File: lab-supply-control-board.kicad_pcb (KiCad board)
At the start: 2 copper layers, 94 x 66 mm, 101 parts, among them J1 0.1" header, J10 USB_B_Micro, J11 0.1" Header, J12 1x04 JST, J13 1x04 JST, J14 0.1" Header, J4 0.1" Header, J5 0.1" Header, J6 AVR-ISP-6, J7 0.1" Header, J8 0.1" Header, J9 0.1" Header, Q1 BSS138, Q2 BSS138, Q3 2N3904, Q4 2N3904, Q5 2N3904, Q6 BSS138, Q7 BSS138, U1 MCP4716AxT-ECH, U2 ATmega328P-AU, U3 24LC04, U4 LM4040DBZ-2.5, U5 MCP4716AxT-ECH, U6 MIC5365-3.3YD5, U7 FT232RL, Y1 Crystal_GND24

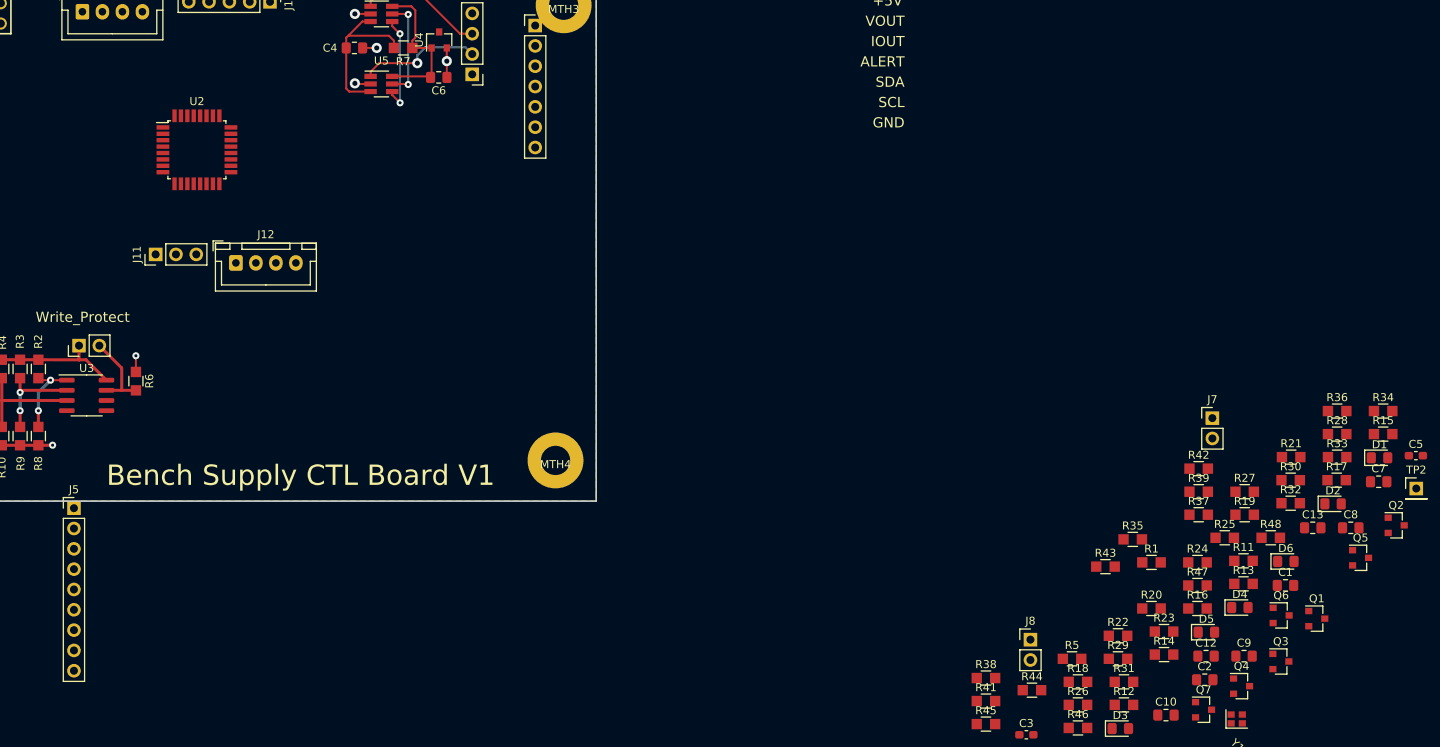
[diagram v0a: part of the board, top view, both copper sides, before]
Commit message: schematic tweak
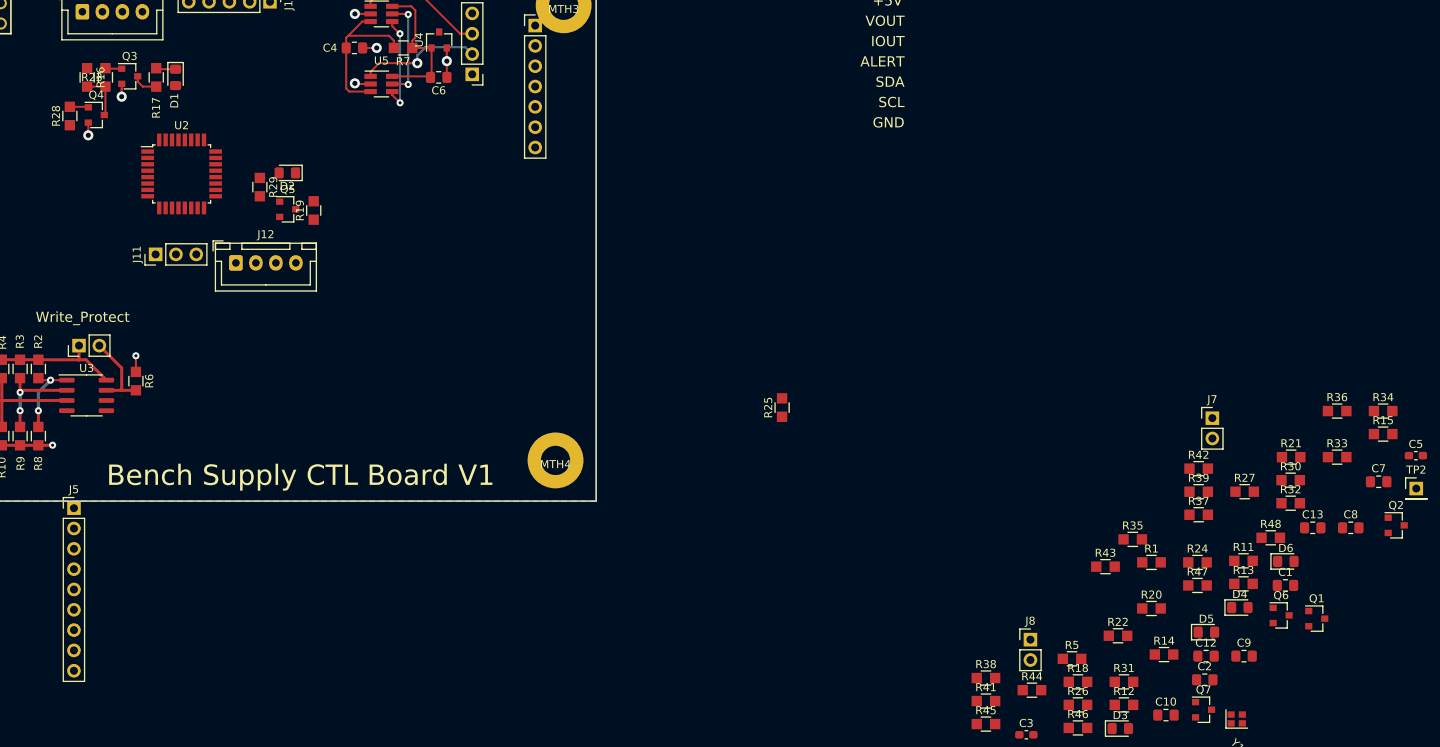
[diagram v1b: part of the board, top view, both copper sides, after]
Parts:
- moved R28 163.3 mm to (101.9, 71.2), turned to 90 degrees
- moved Q3 161.4 mm to (109.3, 66.3)
- moved Q4 160.0 mm to (105.2, 71.1)
- moved D1 157.8 mm to (115.1, 66.4), turned to 270 degrees
- moved R17 155.9 mm to (112.6, 66.4), turned to 90 degrees
- moved R16 153.9 mm to (104.0, 66.4), turned to 270 degrees
- moved R23 149.4 mm to (106.3, 66.4), turned to 90 degrees
- moved Q5 141.0 mm to (129.1, 82.9)
- moved D2 137.1 mm to (129.0, 78.4), turned to 180 degrees
- moved R19 122.4 mm to (132.3, 83.1), turned to 90 degrees
- moved R29 122.4 mm to (125.6, 80.1), turned to 270 degrees
- moved R25 57.7 mm to (190.9, 107.7), turned to 90 degrees
- moved U2 3.57 mm to (115.8, 78.5)
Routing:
- net Net-(Q4-Pad3): track 0.00 -> 5.89 mm
- net Net-(Q3-Pad3): track 0.00 -> 3.23 mm
- net GND: track 17.8 -> 21.0 mm, vias 6 -> 8
- net Net-(D1-Pad1): track 0.00 -> 2.46 mm
- net Net-(Q4-Pad2): track 0.00 -> 2.33 mm
- net Net-(Q3-Pad2): track 0.00 -> 2.06 mm

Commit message: Updates to schematic, started control board layout
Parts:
- removed C10, C9: 1.0u, Rays Footprints:C_0805_HandSoldering
- removed Q1, Q2, Q6: BSS138, Package_TO_SOT_SMD:SOT-23
- removed R11, R12, R13, R14, R34, R35: 10k, Rays Footprints:R_0805_HandSoldering
- removed U6: MIC5365-3.3YD5, Package_TO_SOT_SMD:SOT-23-5
- added C14: 0.1u, Rays Footprints:C_0805_HandSoldering, F.Cu at (154.3, 72.8)
- added J2: JST, Connector_JST:JST_XH_B5B-XH-A_1x05_P2.50mm_Vertical, F.Cu at (107.4, 58.9)
- added J3: JST, Connector_JST:JST_XH_B5B-XH-A_1x05_P2.50mm_Vertical, F.Cu at (87.1, 58.9)
- added MTH5: Mount Hole, Rays Footprints:Mount-Hole-#6, F.Cu at (120.7, 99.1)
- added R49: 1k, Rays Footprints:R_0805_HandSoldering, F.Cu at (99.4, 103.6)
- added U8: MCP6002-xSN, Package_SO:SOP-8_3.9x4.9mm_P1.27mm, F.Cu at (153.4, 66.4)
- R24, R26, R41: value 10k -> 19.4k
- R40: value 0 -> 1k
- moved TP2 188.6 mm to (88.2, 68.4)
- moved D6 176.6 mm to (80.9, 91.2), turned to 90 degrees
- moved R48 173.4 mm to (80.9, 95.5), turned to 270 degrees
- moved C13 172.9 mm to (86.2, 96.9), turned to 180 degrees
- moved Cde 172.1 mm to (100.5, 84.3), turned to 315 degrees
- moved D4 165.7 mm to (85.2, 102.4), turned to 90 degrees
- moved Y1 158.8 mm to (102.6, 82.2), turned to 45 degrees
- moved D3 158.2 mm to (81.7, 102.4), turned to 90 degrees
- moved R47 156.6 mm to (86.8, 116.2), turned to 180 degrees
- moved R33 156.4 mm to (104.0, 108.6), turned to 180 degrees
- moved D5 154.0 mm to (91.2, 116.2)
- moved R46 148.4 mm to (85.2, 106.9), turned to 270 degrees
- moved R32 147.8 mm to (107.6, 102.6), turned to 90 degrees
- moved R15 145.3 mm to (120.7, 108.2), turned to 270 degrees
- moved R45 140.6 mm to (81.7, 106.9), turned to 270 degrees
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- renumbered C5 to Cde
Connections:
- C8 pad 2: Net-(C8-Pad2) -> +3.3V
- J5 pad 3: DISP_RESET_3.3 -> DISP_DC_3.3
- J5 pad 4: DISP_DC_3.3 -> MISO_3.3
- J5 pad 8: MISO_3.3 -> DISP_RESET_3.3
- Q7 pad 1: MOSI_3.3 -> +3.3V
- Q7 pad 2: MOSI_3.3 -> DISP_RESET_3.3
- Q7 pad 3: MOSI -> DISP_RESET
- R36 pad 1: MOSI_3.3 -> DISP_RESET_3.3
- R36 pad 2: 3.3V -> +3.3V
- R37 pad 1: MOSI -> DISP_RESET
- R40 pad 1: Net-(C8-Pad2) -> DISP_CS
- R40 pad 2: +3.3V -> Net-(R40-Pad2)
- R41 pad 2: DISP_RESET_3.3 -> MOSI_3.3
- R42 pad 1: DISP_RESET_3.3 -> MOSI_3.3
- R42 pad 2: DISP_RESET -> MOSI
- R43 pad 2: MOSI_3.3 -> DISP_RESET_3.3
- R44 pad 1: MOSI_3.3 -> DISP_RESET_3.3
- R44 pad 2: MOSI -> DISP_RESET
- TP1 pad 2: VOUT_DAC1 -> /VOUT_DAC1
- TP1 pad 3: VOUT_DAC2 -> /VOUT_DAC2
- U1 pad 1: VOUT_DAC2 -> Net-(U1-Pad1)
- U2 pad 1: (no net) -> Net-(J2-Pad3)
- U2 pad 10: DISP_CS -> Net-(J3-Pad3)
- U2 pad 11: DISP_DC -> Net-(J3-Pad2)
- U2 pad 2: (no net) -> Net-(J2-Pad2)
- U2 pad 30: (no net) -> DISP_CS
- U2 pad 31: (no net) -> DISP_DC
- U2 pad 32: (no net) -> Net-(J2-Pad4)
- U2 pad 9: (no net) -> Net-(J3-Pad4)
- U5 pad 1: VOUT_DAC1 -> Net-(U5-Pad1)
- U7 pad 1: (no net) -> Net-(R40-Pad2)
- U7 pad 17: Net-(C8-Pad2) -> +3.3V
- U7 pad 5: (no net) -> Net-(R49-Pad2)
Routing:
- net +5V: track 36.2 -> 187.3 mm, vias 0 -> 4
- net GND: track 21.0 -> 84.0 mm, vias 8 -> 36
- net Net-(J3-Pad2): track 0.00 -> 47.7 mm
- net RESET: track 0.00 -> 45.9 mm
- net Net-(J3-Pad3): track 0.00 -> 45.0 mm
- net Net-(J3-Pad4): track 0.00 -> 43.9 mm
- net ADC0: track 0.00 -> 26.5 mm
- net ADC1: track 0.00 -> 24.7 mm
- net ADC2: track 0.00 -> 24.2 mm
- net ADC3: track 0.00 -> 24.2 mm
- net Net-(J2-Pad2): track 0.00 -> 21.7 mm
- net Net-(J2-Pad4): track 0.00 -> 21.6 mm
- net Net-(J2-Pad3): track 0.00 -> 21.3 mm
- net DISP_RESET_3.3: track 0.00 -> 20.7 mm
- net SCK: track 0.00 -> 19.7 mm
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- added copper zone on F.Cu, net /VOUT_DAC1
- added copper zone on F.Cu, net /VOUT_DAC2
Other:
- board text added: "3.3V"
- board text added: "5.0V"
- board text added: "ADC3/2/1/0/GND"
- board text added: "DACs --- Buffer"
- board text added: "Encoder1"
- board text added: "Encoder2"
- board text added: "I2C"
- board text added: "Reset"
- board text added: "SCK"
- board text added: "SPI"

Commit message: Updated control sch, first full cut at layout
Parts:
- removed C12: 0.1u, Rays Footprints:C_0805_HandSoldering
- removed R10, R2, R3, R4, R6, R8, R9: 10k, Rays Footprints:R_0805_HandSoldering
- removed U3: 24LC04, Package_SO:SOIC-8_3.9x4.9mm_P1.27mm
- J1: value 0.1" header -> JST; footprint Connector_PinHeader_2.54mm:PinHeader_1x02_P2.54mm_Vertical -> Connector_JST:JST_XH_B2B-XH-A_1x02_P2.50mm_Vertical
- J14: footprint Connector_PinHeader_2.54mm:PinHeader_1x05_P2.54mm_Vertical -> Connector_PinHeader_2.54mm:PinHeader_1x04_P2.54mm_Vertical
- moved C1 89.7 mm to (104.5, 77.6), turned to 90 degrees
- moved S1 89.3 mm to (160.4, 105.5)
- moved C8 82.9 mm to (89.4, 100.6)
- moved TP2 81.5 mm to (156.3, 113.1)
- moved J7 73.3 mm to (77.9, 82.3), turned to 180 degrees
- moved J6 73.3 mm to (146.4, 112.2), turned to 0 degrees
- moved C7 67.4 mm to (98.2, 114.7), turned to 270 degrees
- moved J1 44.4 mm to (125.3, 58.9), turned to 0 degrees
- moved R21 42.6 mm to (147.4, 101.1), turned to 270 degrees
- moved R5 31.6 mm to (149.1, 105.1)
- moved R20 31.5 mm to (150.9, 101.0), turned to 270 degrees
- moved J13 15.6 mm to (145.6, 94.4)
- moved C13 11.5 mm to (97.6, 95.4), turned to 90 degrees
- moved J12 9.16 mm to (131.0, 94.4)
- moved J14 7.62 mm to (143.0, 58.9)
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- renumbered Cde to C5
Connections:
- net VOUT renamed BB_VOUT
- J1 pad 1: +5V -> GND
- J1 pad 2: Net-(J1-Pad2) -> BUTTON
- J13 pad 2: SCL -> SDA
- J13 pad 3: SDA -> SCL
- J4 pad 5: SDA -> SCL
- J4 pad 6: SCL -> SDA
- U2 pad 26: ADC3 -> BUTTON
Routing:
- net +5V: track 187.3 -> 480.1 mm, vias 4 -> 7
- net +3.3V: track 14.8 -> 105.9 mm, vias 0 -> 4
- net RESET: track 45.9 -> 114.0 mm, vias 0 -> 6
- net MISO: track 15.7 -> 81.3 mm, vias 0 -> 1
- net SCK: track 19.7 -> 84.2 mm
- net MOSI: track 15.2 -> 78.5 mm, vias 0 -> 2
- net BB_ALERT: track 0.00 -> 54.5 mm, vias 0 -> 2
- net BB_VOUT: track 0.00 -> 51.3 mm, vias 0 -> 2
- net BB_IOUT: track 0.00 -> 48.4 mm, vias 0 -> 2
- net SCL: track 17.8 -> 63.6 mm, vias 2 -> 4
- net SDA: track 12.4 -> 58.1 mm, vias 2 -> 3
- net DISP_CS: track 0.00 -> 41.3 mm, vias 0 -> 2
- net DISP_DC: track 0.00 -> 40.7 mm, vias 0 -> 2
- net GND: track 84.0 -> 123.3 mm, vias 36 -> 64
- net DISP_RESET: track 5.21 -> 43.2 mm, vias 0 -> 2
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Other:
- rule pad_to_mask_clearance: 0.2032 -> 0.0508
- rule solder_mask_min_width: 0.254 -> 0.2032
- board text added: "ADC2/1/0/GND"
- board text added: "Analog Board"
- board text added: "Bench Supply Control Board V1"
- board text added: "Button"
- board text added: "DAC OUTS"
- board text added: "DISPLAY"
- board text added: "ISP-6"
- board text added: "PB2"
- board text removed: "+5V"
- board text removed: "ADC3/2/1/0/GND"
- board text removed: "ALERT"
- board text removed: "Bench Supply CTL Board V1"
- board text removed: "DACs --- Buffer"
- board text removed: "IOUT"
- board text removed: "SDA"
- board text removed: "VOUT"
- board text removed: "Write_Protect"
- board text removed: "|----| GND"
- board text removed: "|----| Vout"

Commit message: Worked on board layouts
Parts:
- J1: footprint Connector_JST:JST_XH_B2B-XH-A_1x02_P2.50mm_Vertical -> Connector_JST:JST_XH_B4B-XH-A_1x04_P2.50mm_Vertical
- J10: value USB_B_Micro -> USB-Micro; footprint Connector_USB:USB_Micro-B_Molex-105133-0001 -> Rays Footprints:USB-Micro-AMPHENOL_10118194-0001LF
- J14: footprint Connector_PinHeader_2.54mm:PinHeader_1x04_P2.54mm_Vertical -> Connector_JST:JST_XH_B5B-XH-A_1x05_P2.50mm_Vertical
- J4: footprint Connector_PinHeader_2.54mm:PinHeader_1x07_P2.54mm_Vertical -> Connector_JST:JST_XH_B5B-XH-A_1x05_P2.50mm_Vertical
- J5: footprint Connector_PinHeader_2.54mm:PinHeader_1x09_P2.54mm_Vertical -> Connector_JST:JST_XH_B9B-XH-A_1x09_P2.50mm_Vertical
- TP1: footprint Connector_PinHeader_2.54mm:PinHeader_1x04_P2.54mm_Vertical -> Connector_JST:JST_XH_B4B-XH-A_1x04_P2.50mm_Vertical
- U1: value MCP4716AxT-ECH -> MCP4716A0T-ECH
- U5: value MCP4716AxT-ECH -> MCP4716A1T-ECH
- moved Q3 22.5 mm to (96.5, 72.4), turned to 180 degrees
- moved D1 22.3 mm to (96.3, 66.1), turned to 180 degrees
- moved R17 21.4 mm to (96.4, 68.2), turned to 0 degrees
- moved J5 20.2 mm to (122.7, 116.2), turned to 180 degrees
- moved D6 17.6 mm to (78.1, 108.6), turned to 0 degrees
- moved J10 17.1 mm to (75.1, 86.3), turned to 270 degrees
- moved R23 14.9 mm to (100.5, 72.3), turned to 270 degrees
- moved C11 13.5 mm to (84.3, 78.6), turned to 90 degrees
- moved Q4 13.0 mm to (100.9, 67.5), turned to 270 degrees
- moved R48 11.0 mm to (78.1, 106.2), turned to 0 degrees
- moved J9 10.2 mm to (77.9, 100.1)
- moved C7 9.99 mm to (93.0, 106.2), turned to 180 degrees
- moved C8 9.72 mm to (91.1, 91.1), turned to 270 degrees
- moved R40 9.71 mm to (102.1, 100.6)
- moved C13 9.66 mm to (89.0, 91.0)
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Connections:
- net BUTTON renamed BUTTON2
- net Net-(D3-Pad1) renamed /RxLED
- net Net-(D4-Pad1) renamed /TxLED
- J14 pad 1: GND -> ADC3
- J14 pad 2: ADC0 -> ADC2
- J14 pad 4: ADC2 -> ADC0
- J3 pad 1: +5V -> GND
- J3 pad 5: GND -> +5V
- J4 pad 2: BB_VOUT -> BB_ALERT
- J4 pad 3: BB_IOUT -> SCL
- J4 pad 4: BB_ALERT -> SDA
- J4 pad 5: SCL -> GND
- J5 pad 1: +5V -> GND
- J5 pad 2: DISP_CS_3.3 -> DISP_RESET_3.3
- J5 pad 3: DISP_DC_3.3 -> Net-(J5-Pad3)
- J5 pad 4: MISO_3.3 -> SCK_3.3
- J5 pad 6: SCK_3.3 -> MISO_3.3
- J5 pad 7: Net-(J5-Pad7) -> DISP_DC_3.3
- J5 pad 8: DISP_RESET_3.3 -> DISP_CS_3.3
- J5 pad 9: GND -> +5V
- R15 pad 2: Net-(J5-Pad7) -> Net-(J5-Pad3)
- R18 pad 2: Net-(J5-Pad7) -> Net-(J5-Pad3)
- R22 pad 2: Net-(J5-Pad7) -> Net-(J5-Pad3)
- U2 pad 19: BB_IOUT -> ADC3
- U2 pad 22: BB_VOUT -> ADC0
- U2 pad 23: ADC0 -> ADC1
- U2 pad 24: ADC1 -> ADC2
- U2 pad 25: ADC2 -> BUTTON1
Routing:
- net BB_VOUT: track 51.3 -> 0.00 mm, vias 2 -> 0
- net BB_IOUT: track 48.4 -> 0.00 mm, vias 2 -> 0
- net SCL: track 63.6 -> 107.2 mm, vias 4 -> 7
- net ADC3: track 0.00 -> 41.6 mm, vias 0 -> 2
- net +5V: track 480.1 -> 441.2 mm, vias 7 -> 5
- net SDA: track 58.1 -> 89.3 mm, vias 3 -> 4
- net BUTTON1: track 0.00 -> 23.7 mm
- net GND: track 123.3 -> 142.4 mm, vias 64 -> 69
- net USB_D-: track 0.00 -> 17.0 mm, vias 0 -> 2
- net Net-(J5-Pad7): track 16.8 -> 0.00 mm
- net USB_D+: track 0.00 -> 16.7 mm, vias 0 -> 2
- net Net-(J5-Pad3): track 0.00 -> 14.8 mm
- net +3.3V: track 105.9 -> 91.5 mm
- net ADC1: track 29.3 -> 42.0 mm
- net ADC0: track 32.4 -> 44.8 mm
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- added copper zone on F.Cu, net +5V
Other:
- board text added: "ADC3/2/1/0/GND"
- board text added: "Buttons"
- board text added: "Rx"
- board text added: "Tx"
- board text removed: "ADC2/1/0/GND"
- board text removed: "Button"

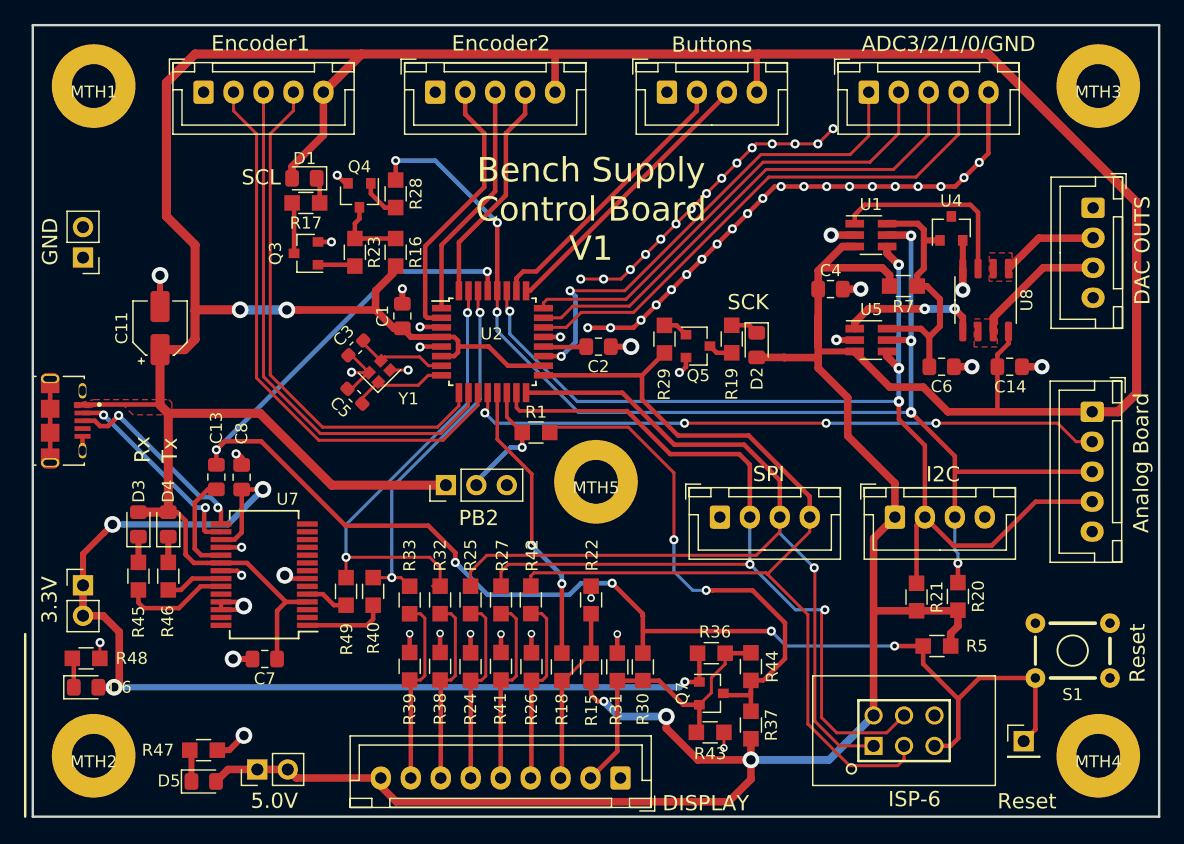
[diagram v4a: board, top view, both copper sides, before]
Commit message: More work on board layouts
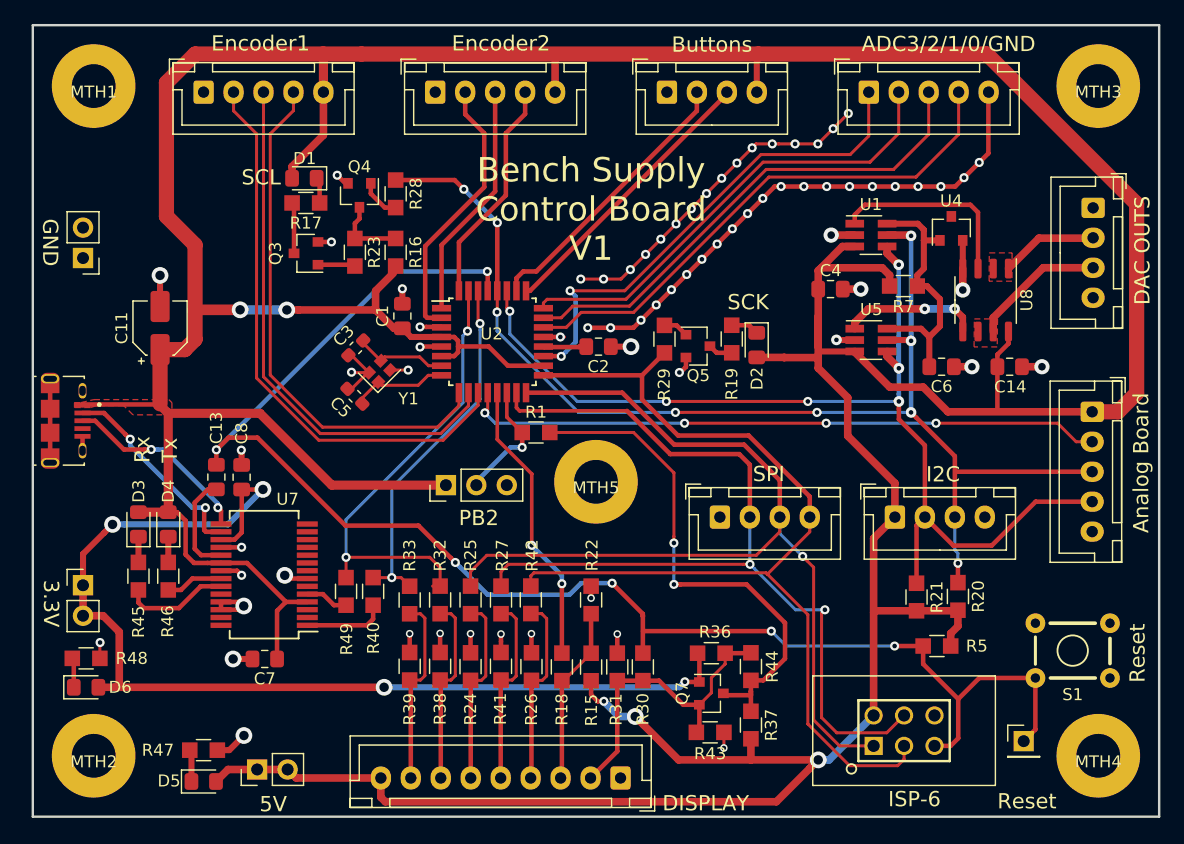
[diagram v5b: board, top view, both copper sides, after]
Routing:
- net +5V: track 441.2 -> 445.0 mm
- net SCL: track 107.2 -> 104.9 mm, vias 7 -> 9
- net GND: track 142.4 -> 144.2 mm, vias 69 -> 70
- net USB_D+: track 16.7 -> 16.0 mm
- net SDA: vias 4 -> 6
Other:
- board text added: "5V"
- board text removed: "5.0V"

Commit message: Lots of updates
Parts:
- moved J4 30.0 mm to (153.3, 114.3), turned to 180 degrees
- moved J6 26.3 mm to (160.4, 89.9), turned to 90 degrees
- moved TP2 14.0 mm to (163.1, 100.8)
- moved D5 2.54 mm to (85.4, 116.4)
- moved J8 2.54 mm to (89.8, 115.4)
- moved R47 2.54 mm to (85.4, 113.8)
- moved J5 2.54 mm to (120.2, 116.2)
- moved C14 1.52 mm to (153.6, 81.8)
- moved S1 1.34 mm to (161.4, 106.5)
- moved J13 1.27 mm to (144.3, 94.4)
- moved Q7 1.27 mm to (129.0, 109.1)
- moved R36 1.27 mm to (129.0, 105.7)
- moved R43 1.27 mm to (128.9, 112.3)
- moved J12 1.27 mm to (129.7, 94.4)
- moved R37 1.27 mm to (132.3, 111.7)
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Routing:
- net +5V: track 445.0 -> 484.3 mm, vias 5 -> 4
- net BB_ALERT: track 53.4 -> 72.4 mm
- net RESET: track 125.8 -> 140.3 mm
- net MISO: track 81.2 -> 88.2 mm, vias 1 -> 5
- net SCL: track 104.9 -> 110.6 mm
- net SDA: track 89.3 -> 93.0 mm
- net DISP_RESET: track 43.5 -> 41.5 mm
- net +3.3V: track 91.3 -> 90.0 mm
- net SCK: track 83.6 -> 84.8 mm, vias 0 -> 2
- net MOSI_3.3: track 15.8 -> 16.9 mm
- net SCK_3.3: track 15.9 -> 16.9 mm
- net Net-(J5-Pad3): track 14.8 -> 15.9 mm
- net MISO_3.3: track 15.8 -> 16.9 mm
- net DISP_DC_3.3: track 15.9 -> 16.9 mm
- net DISP_CS_3.3: track 15.9 -> 16.9 mm
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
